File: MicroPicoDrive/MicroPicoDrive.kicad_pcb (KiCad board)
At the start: 2 copper layers, 66 x 59 mm, 20 parts, among them IC1 SN74LVC1T45DBVR, IC2 SN74LVC1T45DBVR, IC3 TXU0304QPWRQ1, J1 Conn_02x16, J2 QL_CONN, J3 PicoBlade-53261-0371, U2 Pico, U4 AMS1117-5.0

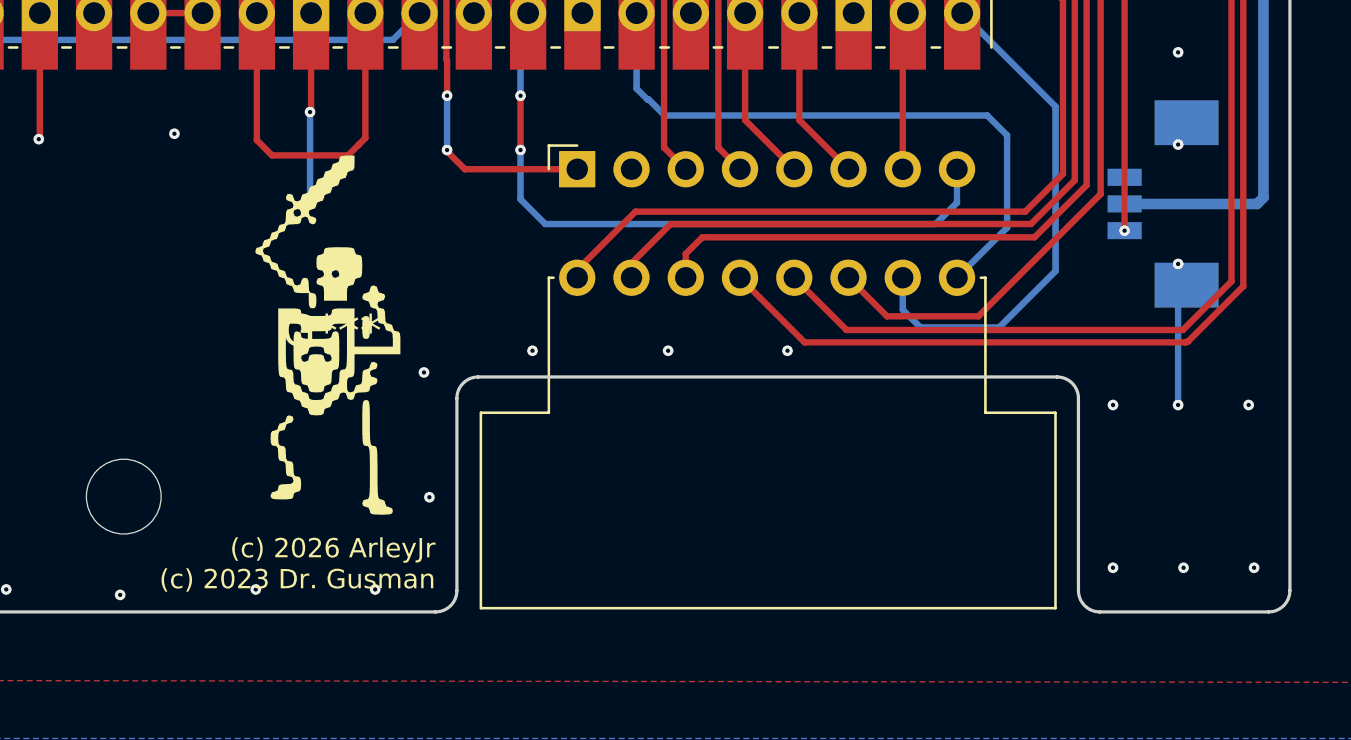
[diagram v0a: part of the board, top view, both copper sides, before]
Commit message: Add mainboard silkscreen labels and cartridge copper zone
Mainboard gains front-silkscreen labelling (KiBuzzard label and text
items); the cartridge PCB gets a new copper pour. Gerbers re-exported
for both boards.
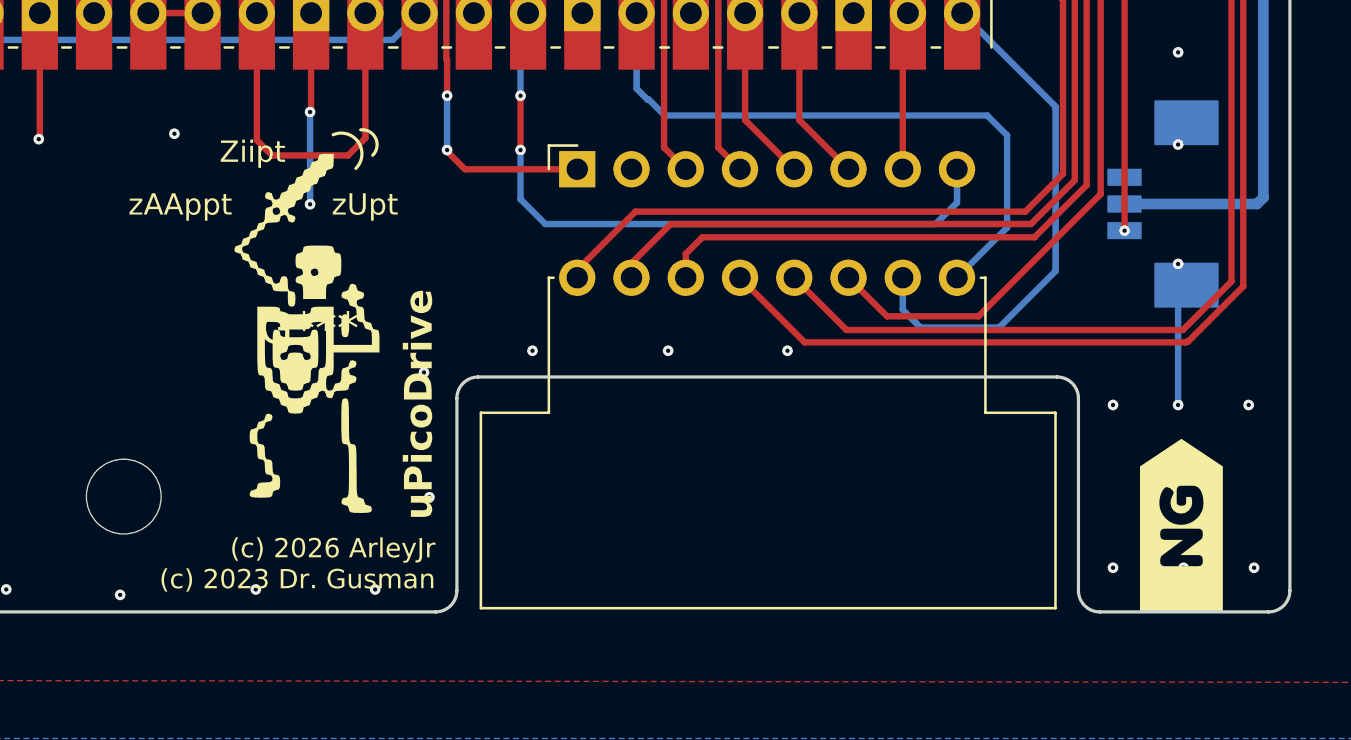
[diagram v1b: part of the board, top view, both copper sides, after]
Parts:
- added kibuzzard-6A718069: G***, kibuzzard-6A718069, F.Cu at (175.2, 127.0)
- moved G*** 0.98 mm to (134.4, 117.9)
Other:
- board text added: "Ziipt"
- board text added: "uPicoDrive"
- board text added: "zAAppt"
- board text added: "zUpt"
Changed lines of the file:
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@@
 		)
+	)
+	(footprint "kibuzzard-6A718069"
+		(layer "F.Cu")
+		(at 175.16 127.05 90)
+		(descr "Generated with KiBuzzard")
+		(tags "kb_params=eyJBbGlnbm1lbnRDaG9pY2UiOiAiQ2VudGVyIiwgIkNhcExlZnRDaG9pY2UiOiAiWyIsICJDYXBSaWdodENob2ljZSI6ICI+IiwgIkZvbnRDb21ib0JveCI6ICJGcmVkZHlTcGFyay1SZWd1bGFyIiwgIkhlaWdodEN0cmwiOiAyLjAsICJMYXllckNvbWJvQm94IjogIkYuU2lsa1MiLCAiTGluZVNwYWNpbmdDdHJsIjogMS41LCAiTXVsdGlMaW5lVGV4dCI6ICJORyIsICJQYWRkaW5nQm90dG9tQ3RybCI6IDMuOCwgIlBhZGRpbmdMZWZ0Q3RybCI6IDkuMCwgIlBhZGRpbmdSaWdodEN0cmwiOiAzLjgsICJQYWRkaW5nVG9wQ3RybCI6IDMuOCwgIldpZHRoQ3RybCI6IDAuMCwgImFkdmFuY2VkQ2hlY2tib3giOiBmYWxzZSwgImlubGluZUZvcm1hdFRleHRib3giOiBmYWxzZSwgImxpbmVvdmVyU3R5bGVDaG9pY2UiOiAiUm91bmRlZCIsICJsaW5lb3ZlclRoaWNrbmVzc0N0cmwiOiAxfQ==")
+		(property "Reference" "kibuzzard-6A718069"
+			(at 0 -4.98696 90)
+			(layer "F.SilkS")
+			(hide yes)
+			(effects
+				(font
+					(size 0.001 0.001)
+				)
+			)
+		)
+		(property "Value" "G***"
+			(at 0 4.98696 90)
+			(layer "F.SilkS")
+			(hide yes)
+			(effects
+				(font
+					(size 0.001 0.001)
+				)
+			)
+		)
+		(property "Datasheet" ""
+			(at 0 0 90)
+			(layer "F.Fab")
+			(hide yes)
+			(effects
+				(font
+					(size 1.27 1.27)
+				)
+			)
+		)
+		(property "Description" ""
+			(at 0 0 90)
+			(layer "F.Fab")
+			(hide yes)
+			(effects
+				(font
+					(size 1.27 1.27)
+				)
+			)
+		)
+		(attr board_only exclude_from_pos_files exclude_from_bom)
+		(duplicate_pad_numbers_are_jumpers no)
+		(fp_poly
+			(pts
+				(xy -1.909076 -1.93896) (xy -4.054999 -1.93896) (xy -4.054999 1.93896) (xy -1.909076 1.93896) (xy -1.651566 1.93896)
+				(xy -1.651566 1.004292) (xy -1.798919 0.984263) (xy -1.876172 0.919886) (xy -1.903354 0.841202)
+				(xy -1.909076 0.741059) (xy -1.909076 -0.74392) (xy -1.903354 -0.839771) (xy -1.874742 -0.915594)
+				(xy -1.796058 -0.97711) (xy -1.645843 -0.995708) (xy -1.515657 -0.978541) (xy -1.442696 -0.942775)
+				(xy -1.391194 -0.88412) (xy -0.675886 0.077253) (xy -0.675886 -0.74392) (xy -0.670164 -0.83834)
+				(xy -0.641551 -0.914163) (xy -0.561437 -0.97568) (xy -0.412653 -0.995708) (xy -0.263869 -0.97568)
+				(xy -0.183755 -0.909871) (xy -0.156573 -0.831187) (xy -0.152281 -0.732475) (xy -0.152281 0.74392)
+				(xy -0.156573 0.842632) (xy -0.183755 0.919886) (xy -0.263869 0.984263) (xy -0.415514 1.004292)
+				(xy -0.562868 0.988555) (xy -0.647274 0.927039) (xy -1.388333 -0.051502) (xy -1.388333 0.74392)
+				(xy -1.392624 0.842632) (xy -1.419806 0.919886) (xy -1.499921 0.984263) (xy -1.651566 1.004292)
+				(xy -1.651566 1.93896) (xy 1.03513 1.93896) (xy 1.03513 1.032904) (xy 0.836274 1.013412) (xy 0.651725 0.954936)
+				(xy 0.481481 0.857475) (xy 0.325544 0.72103) (xy 0.195358 0.557403) (xy 0.102368 0.378398) (xy 0.046574 0.184013)
+				(xy 0.027976 -0.025751) (xy 0.046843 -0.225769) (xy 0.103441 -0.410944) (xy 0.197773 -0.581277)
+				(xy 0.329836 -0.736767) (xy 0.488366 -0.866327) (xy 0.662097 -0.95887) (xy 0.851027 -1.014396) (xy 1.055158 -1.032904)
+				(xy 1.203584 -1.022532) (xy 1.36274 -0.991416) (xy 1.513313 -0.941702) (xy 1.635988 -0.875536) (xy 1.716102 -0.818312)
+				(xy 1.769035 -0.758226) (xy 1.796217 -0.67525) (xy 1.730409 -0.515021) (xy 1.624543 -0.401288) (xy 1.518677 -0.363376)
+				(xy 1.364171 -0.429185) (xy 1.217533 -0.48927) (xy 1.040852 -0.509299) (xy 0.852726 -0.473891) (xy 0.694643 -0.367668)
+				(xy 0.587347 -0.209943) (xy 0.551582 -0.020029) (xy 0.588778 0.175966) (xy 0.700366 0.346209) (xy 0.86131 0.464235)
+				(xy 1.046574 0.503577) (xy 1.211095 0.494278) (xy 1.332698 0.466381) (xy 1.332698 0.220315) (xy 1.120966 0.220315)
+				(xy 1.043713 0.216023) (xy 0.983627 0.193133) (xy 0.934986 0.125894) (xy 0.92068 -0.002861) (xy 0.936417 -0.128755)
+				(xy 0.98935 -0.195994) (xy 1.052297 -0.218884) (xy 1.12955 -0.223176) (xy 1.630265 -0.223176) (xy 1.740423 -0.203147)
+				(xy 1.807662 -0.165951) (xy 1.841997 -0.108727) (xy 1.854872 -0.04578) (xy 1.856303 0.025751) (xy 1.856303 0.612303)
+				(xy 1.787633 0.776824) (xy 1.706803 0.85515) (xy 1.601653 0.921316) (xy 1.443332 0.983309) (xy 1.254491 1.020505)
+				(xy 1.03513 1.032904) (xy 1.03513 1.93896) (xy 1.856303 1.93896) (xy 2.762359 1.93896) (xy 4.054999 0)
+				(xy 2.762359 -1.93896) (xy 1.856303 -1.93896) (xy -1.909076 -1.93896)
+			)
+			(stroke
+				(width 0)
+				(type solid)
+			)
+			(fill yes)
+			(layer "F.SilkS")
+		)
+		(embedded_fonts no)
 	)
 	(footprint "EdgeCon:Edge_connector_02x08"
@@
 	(footprint "LOGO"
 		(layer "F.Cu")
-		(at 135.378874 117.961127)
+		(at 134.398874 117.881128)
 		(property "Reference" "G***"
-			(at 0 0 0)
+			(at -0.083738 -0.036338 0)
 			(layer "F.SilkS")
 			(effects
@@
 	)
 	(gr_arc
+		(start 135.447543 108.758627)
+		(mid 136.63 109.11)
+		(end 136.511415 110.337847)
+		(stroke
+			(width 0.15)
+			(type default)
+		)
+		(layer "F.SilkS")
+	)
+	(gr_arc
+		(start 136.737642 108.529097)
+		(mid 137.43791 108.926649)
+		(end 137.3 109.72)
+		(stroke
+			(width 0.15)
+			(type default)
+		)
+		(layer "F.SilkS")
+	)
+	(gr_arc
 		(start 114.24 73.1)
 		(mid 114.53289 72.39289)
@@
 		)
 	)
+	(gr_text "zAAppt"
+		(at 125.85 112.62 0)
+		(layer "F.SilkS")
+		(effects
+			(font
+				(size 1 1)
+				(thickness 0.15)
+			)
+			(justify left bottom)
+		)
+	)
+	(gr_text "Ziipt"
+		(at 130.12 110.15 0)
+		(layer "F.SilkS")
+		(effects
+			(font
+				(size 1 1)
+				(thickness 0.15)
+			)
+			(justify left bottom)
+		)
+	)
+	(gr_text "zUpt"
+		(at 135.37 112.62 0)
+		(layer "F.SilkS")
+		(effects
+			(font
+				(size 1 1)
+				(thickness 0.15)
+			)
+			(justify left bottom)
+		)
+	)
+	(gr_text "uPicoDrive"
+		(at 140.22 126.79 90)
+		(layer "F.SilkS")
+		(effects
+			(font
+				(size 1.3 1.3)
+				(thickness 0.26)
+				(bold yes)
+			)
+			(justify left bottom)
+		)
+	)

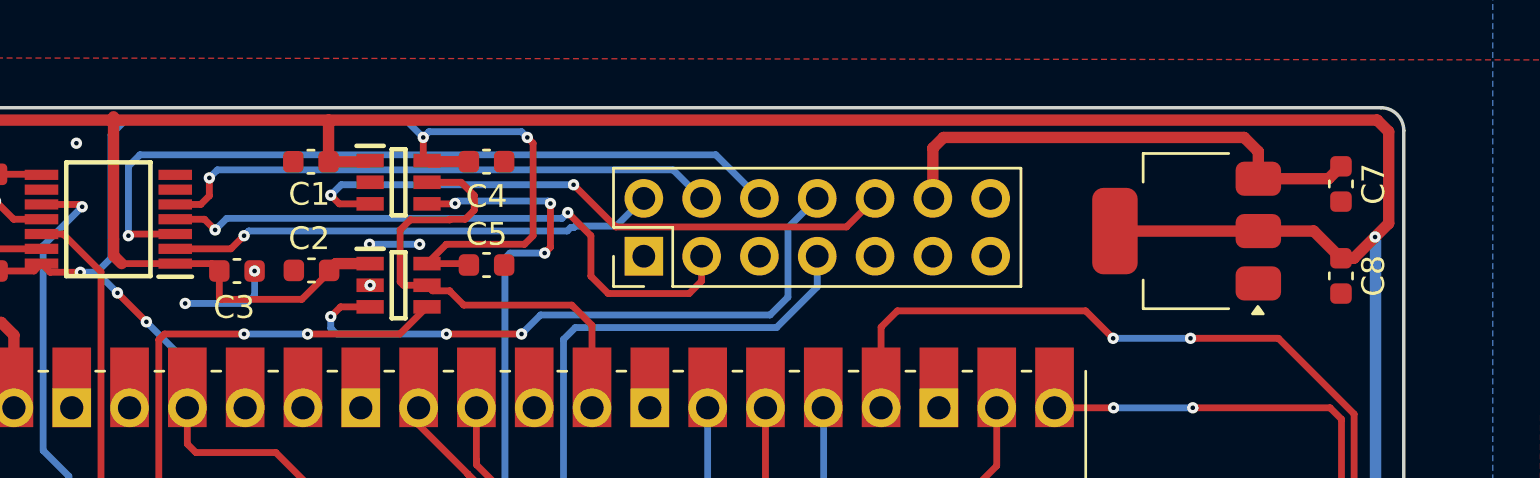
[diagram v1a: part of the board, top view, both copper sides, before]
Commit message: Change C7 and C8 to 0805 hand-solder footprints
The two capacitors move from C_0603_1608Metric to
C_0805_2012Metric_Pad1.18x1.45mm_HandSolder in both the schematic
and the board. Gerbers and drill files are regenerated from the
updated board, and the DRC silkscreen text height, thickness and
back-layer mirroring checks are set to ignore.
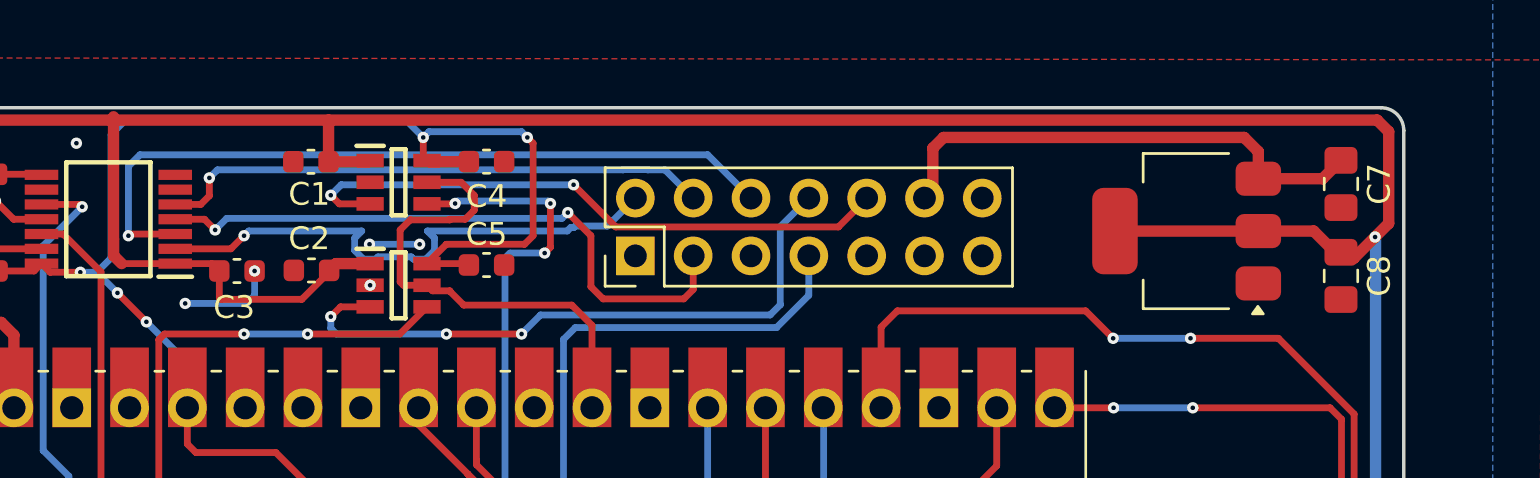
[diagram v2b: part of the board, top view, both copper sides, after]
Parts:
- C7, C8: footprint Capacitor_SMD:C_0603_1608Metric -> Capacitor_SMD:C_0805_2012Metric_Pad1.18x1.45mm_HandSolder
- moved J2 0.37 mm to (146.5, 78.6)
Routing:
- net /QL_CS_IN: track 21.6 -> 24.5 mm
